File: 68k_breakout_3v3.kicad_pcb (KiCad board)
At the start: 2 copper layers, 69.2 x 85.1 mm, 4 parts, among them J1 Conn_02x32_Odd_Even, J2 Conn_02x02_Odd_Even, U1 68000D_PLUG, U2 68000D

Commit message: Initial layout complete
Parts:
- added C1: 100n, Capacitor_SMD:C_0805_2012Metric_Pad1.18x1.45mm_HandSolder, F.Cu at (78.2, 91.2)
- added C10: 1u, Capacitor_SMD:C_0805_2012Metric_Pad1.18x1.45mm_HandSolder, F.Cu at (104.0, 102.3)
- added C2: 100n, Capacitor_SMD:C_0805_2012Metric_Pad1.18x1.45mm_HandSolder, F.Cu at (78.2, 124.9)
- added C3: 100n, Capacitor_SMD:C_0805_2012Metric_Pad1.18x1.45mm_HandSolder, F.Cu at (78.1, 105.3)
- added C4: 100n, Capacitor_SMD:C_0805_2012Metric_Pad1.18x1.45mm_HandSolder, F.Cu at (129.8, 124.8)
- added C5: 100n, Capacitor_SMD:C_0805_2012Metric_Pad1.18x1.45mm_HandSolder, F.Cu at (129.8, 109.9)
- added C6: 100n, Capacitor_SMD:C_0805_2012Metric_Pad1.18x1.45mm_HandSolder, F.Cu at (129.6, 94.3)
- added C7: 100n, Capacitor_SMD:C_0805_2012Metric_Pad1.18x1.45mm_HandSolder, F.Cu at (78.0, 80.9)
- added C8: 100n, Capacitor_SMD:C_0805_2012Metric_Pad1.18x1.45mm_HandSolder, F.Cu at (77.8, 71.0)
- added C9: 1u, Capacitor_SMD:C_0805_2012Metric_Pad1.18x1.45mm_HandSolder, F.Cu at (106.3, 102.3)
- added IC1: SN74CB3T3245DW, Package_SO:TSSOP-20_4.4x6.5mm_P0.65mm, F.Cu at (78.0, 86.0)
- added IC2: SN74CB3T3245DW, Package_SO:TSSOP-20_4.4x6.5mm_P0.65mm, F.Cu at (78.0, 120.0)
- added IC3: SN74CB3T3245DW, Package_SO:TSSOP-20_4.4x6.5mm_P0.65mm, F.Cu at (78.0, 100.0)
- added IC4: SN74CB3T3245DW, Package_SO:TSSOP-20_4.4x6.5mm_P0.65mm, F.Cu at (130.0, 130.0)
- added IC5: SN74CB3T3245DW, Package_SO:TSSOP-20_4.4x6.5mm_P0.65mm, F.Cu at (130.0, 115.0)
- added IC6: SN74CB3T3245DW, Package_SO:TSSOP-20_4.4x6.5mm_P0.65mm, F.Cu at (130.0, 100.0)
- added IC7: SN74CB3T3245DW, Package_SO:TSSOP-20_4.4x6.5mm_P0.65mm, F.Cu at (78.0, 76.0)
- added IC8: SN74CB3T3245DW, Package_SO:TSSOP-20_4.4x6.5mm_P0.65mm, F.Cu at (78.0, 66.0)
- added J3: Conn_02x20_Odd_Even, Connector_PinHeader_2.54mm:PinHeader_2x20_P2.54mm_Vertical, F.Cu at (142.0, 130.0)
- added J4: Conn_02x20_Odd_Even, Connector_PinHeader_2.54mm:PinHeader_2x20_P2.54mm_Vertical, F.Cu at (64.0, 130.0)
- added RN1: 10k, Resistor_SMD:R_Array_Convex_4x0603, F.Cu at (133.0, 87.5)
- added RN2: 10k, Resistor_SMD:R_Array_Convex_4x0603, F.Cu at (133.1, 81.5)
- added U3: LM1117-3.3, Package_TO_SOT_SMD:SOT-223-3_TabPin2, F.Cu at (104.0, 95.1)
- J1: value Conn_02x32_Odd_Even -> Conn_02x02_Odd_Even; footprint Connector_PinHeader_2.54mm:PinHeader_2x32_P2.54mm_Vertical -> Connector_PinSocket_2.54mm:PinSocket_2x02_P2.54mm_Vertical
- moved U2 14.3 mm to (94.0, 60.0)
- moved J2 11.2 mm to (127.3, 70.1)
- moved J1 9.89 mm to (127.3, 60.2)
- moved U1 1.70 mm to (90.0, 60.0)
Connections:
- J1 pad 1: /D4 -> +3V3
- J1 pad 2: /D5 -> +3V3
- J1 pad 3: /D3 -> GND
- J1 pad 4: /D6 -> GND
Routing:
- net +3V3: track 0.00 -> 226.7 mm
- net /OE_C_2: track 0.00 -> 148.2 mm, vias 0 -> 1
- net /OE_C_3: track 0.00 -> 142.2 mm, vias 0 -> 4
- net /OE_C_1: track 0.00 -> 137.9 mm, vias 0 -> 4
- net /OE_D_L: track 0.00 -> 120.7 mm, vias 0 -> 3
- net /OE_D_U: track 0.00 -> 109.0 mm, vias 0 -> 3
- net /OE_A_L: track 0.00 -> 55.3 mm, vias 0 -> 1
- net /BGACK: track 58.4 -> 12.8 mm
- net /IPL1: track 58.4 -> 13.1 mm
- net +5V: track 129.1 -> 84.1 mm, vias 2 -> 1
- net /OE_A_M: track 0.00 -> 44.8 mm, vias 0 -> 1
- net /BG: track 58.4 -> 13.8 mm
- net /IPL2: track 58.4 -> 13.9 mm
- net /IPL0: track 58.4 -> 13.9 mm
- net /CLK: track 58.4 -> 14.0 mm
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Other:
- board size 69.2 x 85.1 mm -> 84 x 85.1 mm
- board text added: "3V3"

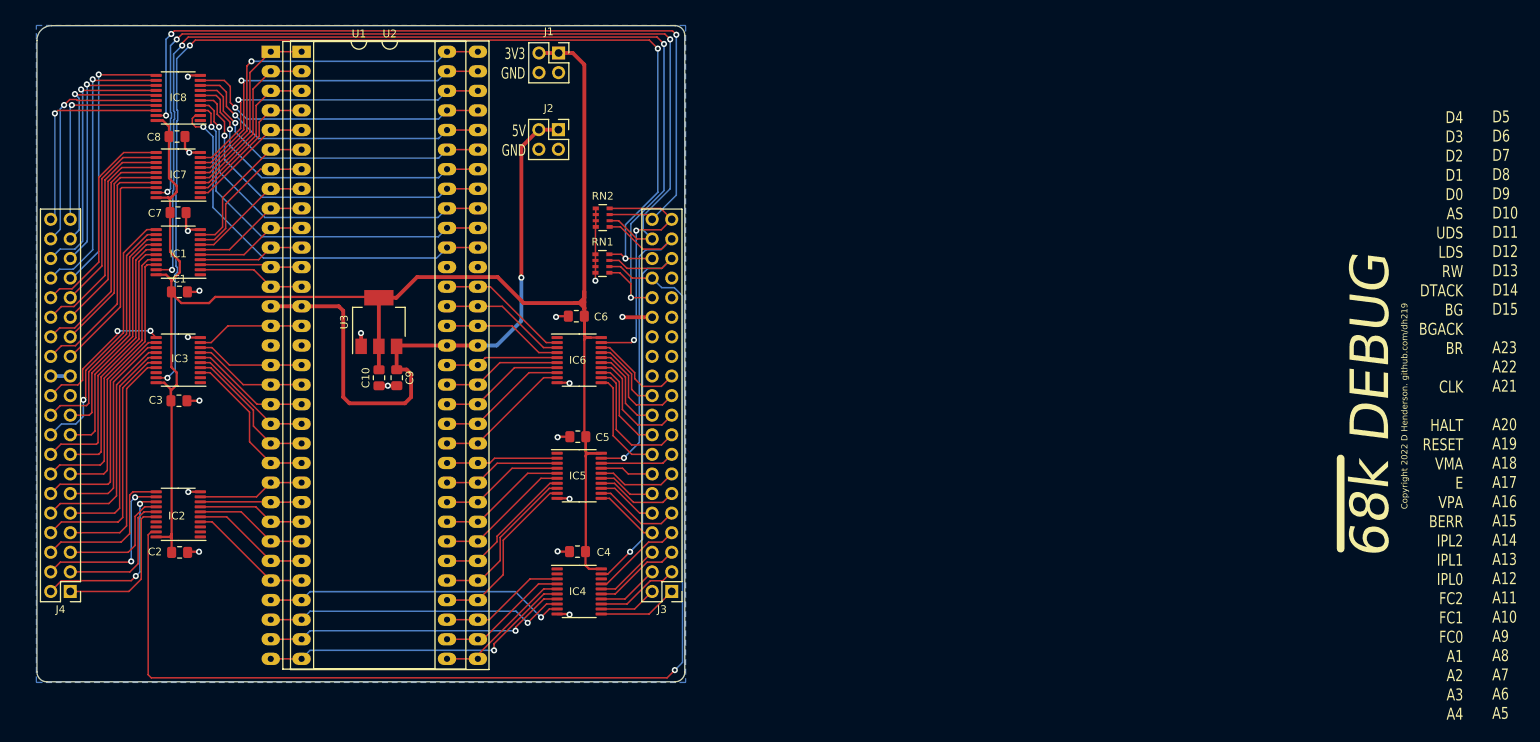
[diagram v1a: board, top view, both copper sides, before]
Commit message: Tweaked layout to better fit. Passes DRC
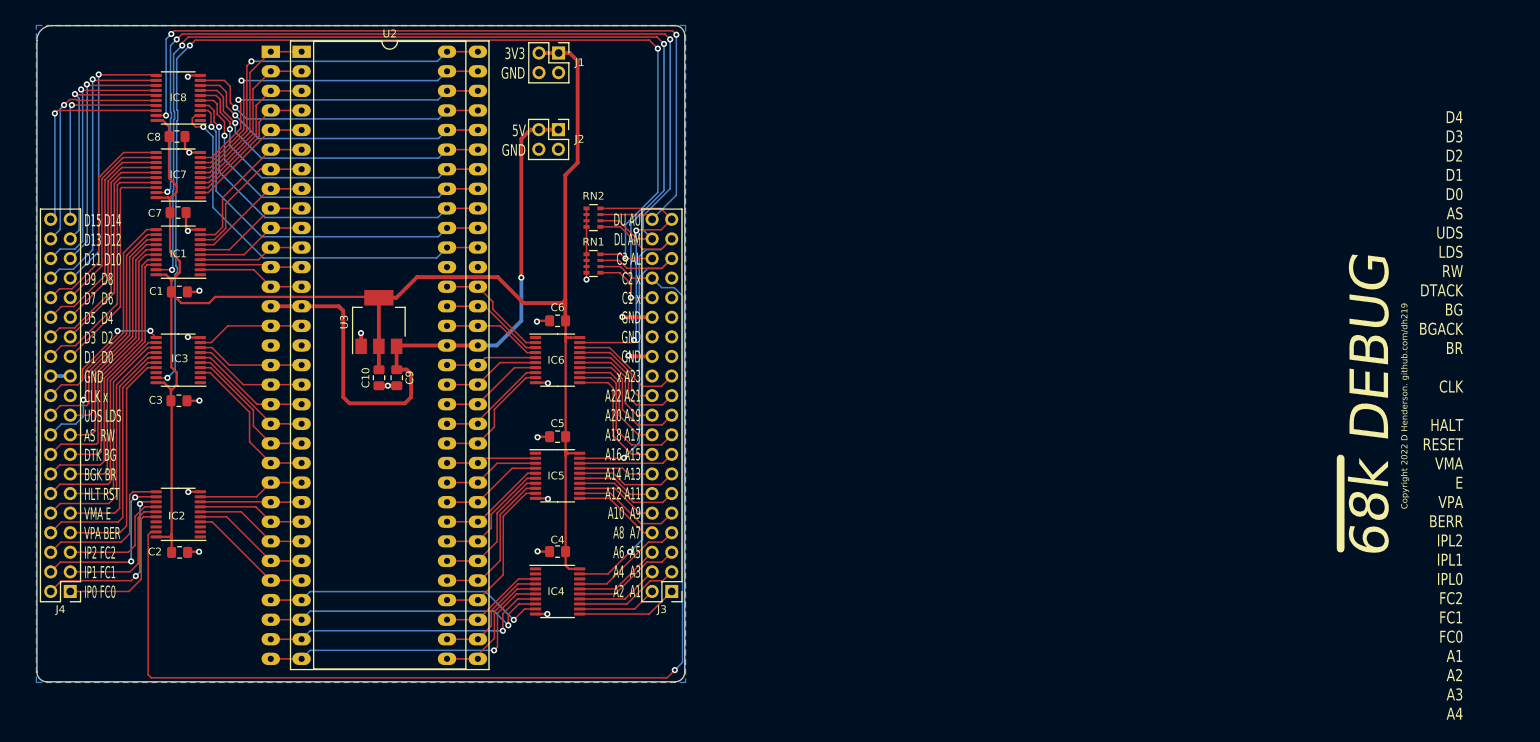
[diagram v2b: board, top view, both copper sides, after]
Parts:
- moved IC4 2.80 mm to (127.2, 130.0)
- moved IC5 2.80 mm to (127.2, 115.0)
- moved IC6 2.80 mm to (127.2, 100.0)
- moved C5 2.62 mm to (127.2, 109.9)
- moved C4 2.58 mm to (127.2, 124.8)
- moved C6 2.50 mm to (127.2, 94.9)
- moved RN2 1.20 mm to (131.8, 81.5)
- moved RN1 1.16 mm to (131.8, 87.5)
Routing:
- net +3V3: track 226.7 -> 215.4 mm
- net /OE_A_U: track 32.5 -> 36.7 mm
- net /OE_A_M: track 44.8 -> 49.0 mm
- net /OE_A_L: track 55.3 -> 59.3 mm
- net /_A17: track 16.8 -> 19.6 mm
- net /_A10: track 7.93 -> 10.7 mm
- net /_A8: track 8.44 -> 11.2 mm
- net /_A7: track 11.9 -> 14.7 mm
- net /_A6: track 8.57 -> 11.4 mm
- net /_A4: track 8.05 -> 10.9 mm
- net /_A3: track 10.9 -> 13.7 mm
- net /_A23: track 12.2 -> 15.0 mm
- net /_A20: track 11.4 -> 14.2 mm
- net /_A2: track 7.54 -> 10.3 mm
- net /_A19: track 15.1 -> 17.9 mm
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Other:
- board text added: "D15 D14 D13 D12 D11 D10 D9 D8 D7 D6 D5 D4 D3 D2 D1 D0 GND CLK x UDS LDS AS RW DTK BG BGK BR HLT RST VMA E VPA BER IP2 FC2 IP1 FC1 IP0 FC0"
- board text added: "DU AU DL AM C3 AL C2 x C1 x GND GND GND x A23 A22 A21 A20 A19 A18 A17 A16 A15 A14 A13 A12 A11 A10 A9 A8 A7 A6 A5 A4 A3 A2 A1"
- board text removed: "D5 D6 D7 D8 D9 D10 D11 D12 D13 D14 D15 A23 A22 A21 A20 A19 A18 A17 A16 A15 A14 A13 A12 A11 A10 A9 A8 A7 A6 A5"

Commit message: Adding copyright
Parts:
- moved U1 4.00 mm to (94.0, 60.0)
- moved U2 4.00 mm to (90.0, 60.0)
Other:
- board text added: "Copyright 2023 D Henderson github.com/dh219"
- board text added: "~{68k BREAKOUT 3V3}"
- board text removed: "Copyright 2022 D Henderson. github.com/dh219"
- board text removed: "D4 D3 D2 D1 D0 AS UDS LDS RW DTACK BG BGACK BR CLK HALT RESET VMA E VPA BERR IPL2 IPL1 IPL0 FC2 FC1 FC0 A1 A2 A3 A4"
- board text removed: "~{68k} DEBUG"
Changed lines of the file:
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@@
   (net 151 "unconnected-(J4-Pad21)")
   (footprint "Package_DIP:DIP-64_W22.86mm_LongPads" (layer "F.Cu")
-    (at 90 60)
+    (at 94 60)
     (descr "64-lead though-hole mounted DIP package, row spacing 22.86 mm (900 mils), LongPads")
     (tags "THT DIP DIL PDIP 2.54mm 22.86mm 900mil LongPads")
@@
   )
   (footprint "Package_DIP:DIP-64_W22.86mm_Socket_LongPads" (layer "F.Cu")
-    (at 94 60)
+    (at 90 60)
     (descr "64-lead though-hole mounted DIP package, row spacing 22.86 mm (900 mils), Socket, LongPads")
     (tags "THT DIP DIL PDIP 2.54mm 22.86mm 900mil Socket LongPads")
@@
     (effects (font (size 1.575 0.8) (thickness 0.15)) (justify right))
   )
-  (gr_text "Copyright 2022 D Henderson. github.com/dh219" (at 237.035 105.955 90) (layer "F.SilkS")
-    (effects (font (size 0.8 0.8) (thickness 0.15)))
+  (gr_text "Copyright 2023 D Henderson\ngithub.com/dh219" (at 60.945 139.335) (layer "F.SilkS")
+    (effects (font (size 0.8 0.8) (thickness 0.15)) (justify left))
   )
   (gr_text "3V3" (at 123 60.26) (layer "F.SilkS")
@@
     (effects (font (size 1.5 1) (thickness 0.25)) (justify right))
   )
-  (gr_text "~{68k} DEBUG" (at 232.59 105.955 90) (layer "F.SilkS")
-    (effects (font (size 5 5) (thickness 1) italic))
-  )
-  (gr_text "D4\nD3\nD2\nD1\nD0\nAS\nUDS\nLDS\nRW\nDTACK\nBG\nBGACK\nBR\n\nCLK\n\nHALT\nRESET\nVMA\nE\nVPA\nBERR\nIPL2\nIPL1\nIPL0\nFC2\nFC1\nFC0\nA1\nA2\nA3\nA4" (at 244.655 107.225) (layer "F.SilkS")
-    (effects (font (size 1.55 1.2) (thickness 0.2)) (justify right))
+  (gr_text "~{68k BREAKOUT 3V3}" (at 74.345 136.39) (layer "F.SilkS")
+    (effects (font (size 2.2 1.8) (thickness 0.4) italic))
   )
   (gr_text "D15 D14\nD13 D12\nD11 D10\nD9  D8\nD7  D6\nD5  D4\nD3  D2\nD1  D0\nGND\nCLK x\nUDS LDS\nAS  RW\nDTK BG\nBGK BR\nHLT RST\nVMA E\nVPA BER\nIP2 FC2\nIP1 FC1\nIP0 FC0\n" (at 65.8 106) (layer "F.SilkS")

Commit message: Minor tweaks pre-gerberisation
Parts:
- J1, J2: footprint Connector_PinSocket_2.54mm:PinSocket_2x02_P2.54mm_Vertical -> Connector_PinHeader_2.54mm:PinHeader_2x02_P2.54mm_Vertical
- moved J1 2.38 mm to (125.0, 60.2)
- moved J2 2.38 mm to (124.9, 70.1)
